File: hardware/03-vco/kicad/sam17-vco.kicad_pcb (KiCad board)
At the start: 2 copper layers, 240 x 172 mm, 140 parts, among them J1 Molex_KK-254_AE-6410-04A_1x04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, J2 IDC-Header_2x06_P2.54mm_Verti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, U1 QFN-32-1EP_4x4mm_P0.4mm_EP2.6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, U10 SOIC-14_3.9x8.7mm_P1.27mm, U11 SOT-89-3, U12 SOT-223-3_TabPin2, U13 VSSOP-8_3x3mm_P0.65mm, U14 SOT-23-5, U2 QFN-32-1EP_4x4mm_P0.4mm_EP2.6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, U3 QFN-32-1EP_4x4mm_P0.4mm_EP2.6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, U4 QFN-32-1EP_4x4mm_P0.4mm_EP2.6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, U5 TSSOP-16_4.4x5mm_P0.65mm, U6 TSSOP-16_4.4x5mm_P0.65mm, U7 TSSOP-16_4.4x5mm_P0.65mm, U8 SOIC-8_3.9x4.9mm_P1.27mm, U9 SOIC-14_3.9x8.7mm_P1.27mm

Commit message: Modulo 3 VCO: cuadro 2x2 y ruteo con Freerouting (Tarea 6, ronda 2)
La causa raiz de la tanda anterior era el desparramo: 4 voces en fila sobre
240x172 mm dejaban el DAC de tono a 85 mm de la voz mas lejana -- 70% por
encima de los 50 mm que modela dac_local_budget.LARGO_LOCAL -- y creaban los
cuellos de ruteo de propina. Aqui las voces van en CUADRO 2x2 con los tres
DAC y la referencia en el hueco central: las cuatro quedan a la misma
distancia, el peor par baja a 41.8 mm (37.7 el de U5, el que manda la
afinacion) y la placa cabe en 114x118 mm, 3.1x menos area. El suelo de
afinacion pasa de 0.635 a 0.5665 cents contra el limite de 0.7.

La fila de abajo va girada 180 grados, y no por simetria: cada lado del QFN
lleva senales fijas, y girando las voces 2 y 4 los cuatro R_MIX y R_PITCH
miran al centro (5 buses ganados) contra VREF_2V5 y PWM_CV que pasan afuera.

El ruteador casero de caminos en L/Z se va entero (~230 lineas) y lo
sustituye Freerouting headless: exportar DSN desde pcbnew, correr el jar,
importar el SES, repetir desde el resultado anterior y quedarse con la mejor
ronda. Tres cosas que costaron encontrarse y quedan documentadas en el
script: -mt 1 es obligatorio (su optimizador multihilo esta roto y admite
estarlo), la 2.2.x/2.3.0 piden Java 25, y el FANOUT viene apagado de fabrica
-- encenderlo, con todo lo demas igual, bajo los tramos sin cerrar de 31 a
11. Como no hay flag de CLI para eso, ajustes_freerouting() parchea las tres
claves que importan del freerouting.json del usuario.

coser_masas() baja cada pad de masa al plano con su propia via DESPUES de
rutear: todo el cobre es SMD en F.Cu y sin via un pad de GNDA mira el
vertido sin tocarlo. Metidas antes del router, esas vias multiplican por
doce el tiempo de cada pasada sin aportar nada al ruteo de senal.

NO CIERRA, y el script sale con error: quedan 18 conexiones de ~500 y el
plano analogico acaba en 30 islas con el 96.5% del cobre en la mayor. Las
dos cosas son el mismo problema y esta acotado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
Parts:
- moved C26 173.4 mm to (64.0, 92.0)
- moved TP2 168.3 mm to (64.0, 96.0)
- moved C25 159.7 mm to (70.0, 92.0)
- moved TP1 152.2 mm to (70.0, 96.0)
- moved H4 137.1 mm to (108.0, 112.0)
- moved J1 136.3 mm to (94.0, 108.0)
- moved C8 132.3 mm to (78.0, 92.0)
- moved C9 127.8 mm to (98.0, 100.0)
- moved U11 127.8 mm to (84.0, 92.0)
- moved H2 126.0 mm to (108.0, 6.00)
- moved C10 125.6 mm to (89.0, 92.0)
- moved U12 123.7 mm to (98.0, 93.0)
- moved TP3 122.8 mm to (78.0, 96.0)
- moved TP4 120.8 mm to (86.0, 100.0)
- moved R_SCALE4 118.1 mm to (83.0, 77.0), turned to 180 degrees
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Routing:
- net GNDA: track 0.00 -> 311.0 mm, vias 0 -> 97
- net PWM_CV: track 0.00 -> 238.1 mm, vias 0 -> 10
- net -12V: track 66.0 -> 302.6 mm, vias 0 -> 10
- net VREF_2V5: track 178.8 -> 395.6 mm, vias 0 -> 12
- net +5V_LOC: track 133.3 -> 338.8 mm, vias 2 -> 16
- net SPI_SCLK: track 0.00 -> 186.6 mm, vias 0 -> 5
- net MIX_SINE: track 52.0 -> 220.6 mm, vias 2 -> 8
- net SPI_CS3: track 0.00 -> 167.8 mm, vias 0 -> 8
- net SQ_3: track 0.00 -> 158.1 mm, vias 0 -> 5
- net VOICE_OUT_1: track 190.1 -> 39.0 mm, vias 2 -> 1
- net CV_PITCH_3: track 6.29 -> 144.4 mm, vias 0 -> 2
- net SPI_MOSI: track 0.00 -> 112.7 mm, vias 0 -> 4
- net SQ_1: track 0.00 -> 111.0 mm, vias 0 -> 3
- net SQ_4: track 0.00 -> 104.9 mm, vias 0 -> 2
- net CV_PITCH_2: track 6.29 -> 86.6 mm, vias 0 -> 4
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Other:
- board size 240 x 172 mm -> 114 x 118 mm

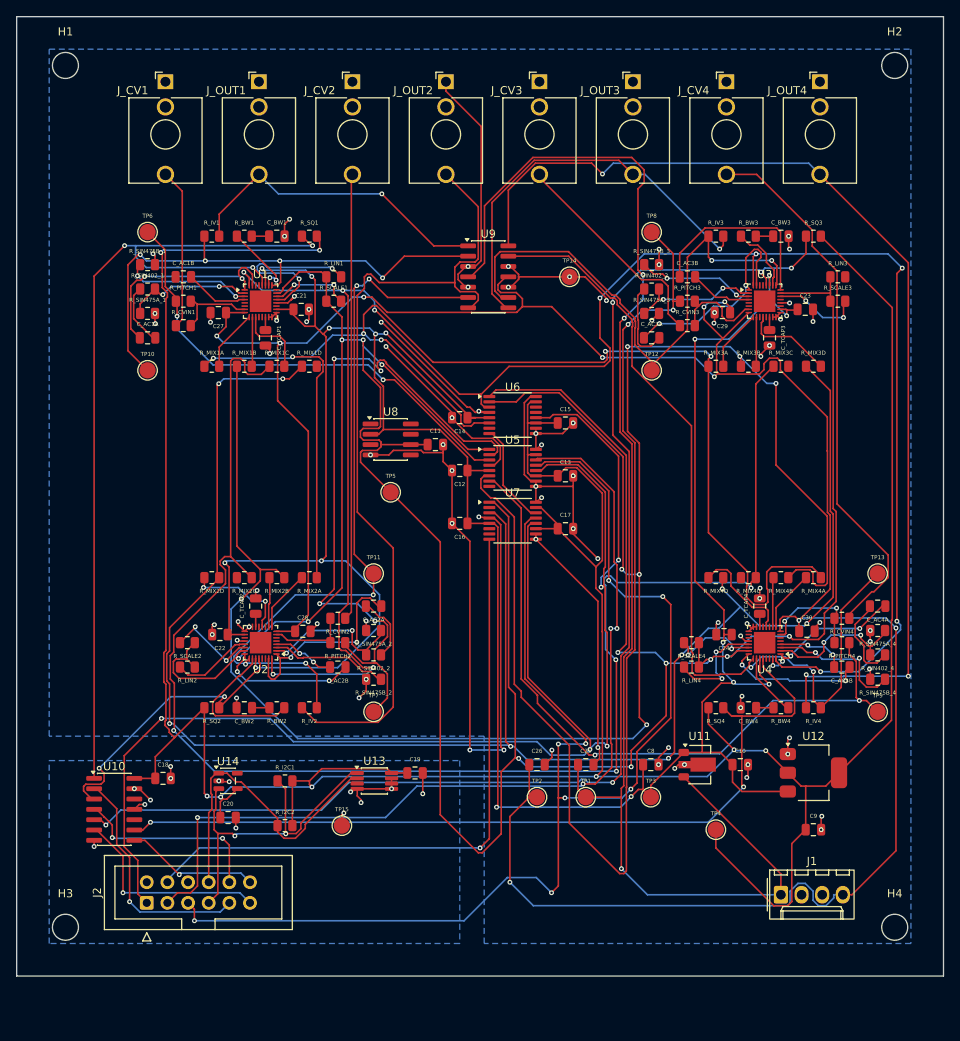
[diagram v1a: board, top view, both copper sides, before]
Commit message: Modulo 3 VCO: la placa pasa a 4 capas (Tarea 6, ronda 3)
Ruling del controlador sobre el BLOCKED de la ronda anterior. La evidencia
de las once configuraciones medidas mostraba que el grafo de esta placa no
es plano y que en 2 capas la unica capa donde cruzar era el propio plano de
masa: cada cruce, una ranura. Ni el spec ni ninguna asercion exigian 2
capas -- era calco de placas mas simples.

El stackup nuevo:

    F.Cu     senal
    In1.Cu   GNDA solida, sin una sola pista
    In2.Cu   GNDD (la esquina de la isla) + potencia
    B.Cu     senal

Y el presupuesto MEJORA con el cambio, no solo el ruteo: dac_local_budget.py
modela el camino DAC->VCO sobre un vertido de 20 mm de ancho, y lo que hay
ahora debajo de ese camino es una capa interna entera y sin cortes. La
asimetria vieja de B.Cu se va con el motivo que la sostenia; la regla nueva
es que In1 no se toca, y se comprueba por partida doble: cero pistas en In1,
y la isla mayor del vertido con mas del 99% del cobre.

Tres cosas que costaron encontrarse y quedan documentadas en el script:

- Un area de reglas de KiCad sobre In1 no vale: se exporta como wire_keepout
  de placa entera y Freerouting se atasca en seco, 200 conexiones sin rutear
  desde la pasada 4 hasta la 139 sin moverse. Lo que si entiende es el
  idioma de Specctra, marcar la capa como (type power); con eso baja de 222
  a 80 en 14 pasadas. Como KiCad no sabe exportar eso, _ajustar_dsn() lo
  parchea en el DSN temporal.
- El router redondea y dejaba pistas a 0.1480 mm apuntando a 0.15: una
  infraccion de DRC por aritmetica. El mismo parche le pide 0.16 mientras el
  DRC sigue exigiendo 0.15.
- El anillo de la voz venia demasiado apretado del apuro de 2 capas y seis
  conexiones locales del QFN no encontraban salida. Con 4 capas hay sitio
  para pagarlo: la celda pasa de 26.4x20.1 a 28.7x22.3 mm.

coser_masas() tenia cuatro bugs, y el ultimo es el que importa: daba por
resuelto un pad que tuviera una via de su red a menos de 1.2 mm. Cercania no
es 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
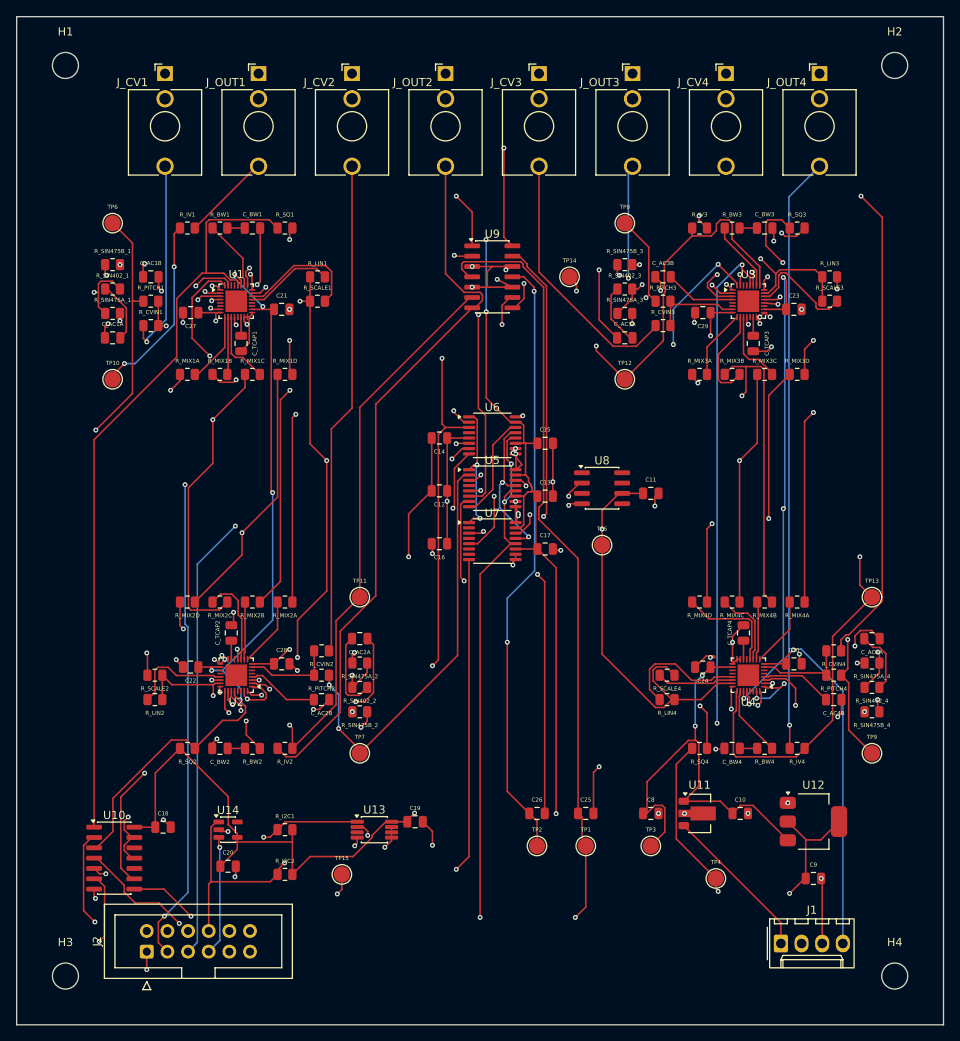
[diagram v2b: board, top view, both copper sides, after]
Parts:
- moved C11 27.2 mm to (78.0, 58.6)
- moved TP5 26.8 mm to (72.0, 65.0)
- moved U8 26.7 mm to (72.0, 58.0)
- moved C10 6.00 mm to (89.0, 98.0)
- moved C18 6.00 mm to (18.0, 99.7)
- moved C19 6.00 mm to (49.0, 99.0)
- moved C20 6.00 mm to (26.0, 104.5)
- moved C25 6.00 mm to (70.0, 98.0)
- moved C26 6.00 mm to (64.0, 98.0)
- moved C8 6.00 mm to (78.0, 98.0)
- moved C9 6.00 mm to (98.0, 106.0)
- moved H3 6.00 mm to (6.00, 118.0)
- moved H4 6.00 mm to (108.0, 118.0)
- moved J1 6.00 mm to (94.0, 114.0)
- moved J2 6.00 mm to (16.0, 115.0)
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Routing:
- net GNDA: track 311.0 -> 154.2 mm, vias 97 -> 71
- net VREF_2V5: track 395.6 -> 257.8 mm, vias 12 -> 9
- net MIX_SAW: track 238.3 -> 136.3 mm, vias 7 -> 4
- net MIX_SINE: track 220.6 -> 131.8 mm, vias 8 -> 4
- net CV_PITCH_3: track 144.4 -> 58.9 mm
- net +3V3_LOC: track 399.3 -> 321.1 mm
- net SPI_SCLK: track 186.6 -> 111.0 mm, vias 5 -> 4
- net SPI_CS3: track 167.8 -> 108.8 mm, vias 8 -> 3
- net MIX_PULSE: track 188.2 -> 135.3 mm, vias 4 -> 3
- net +5V_LOC: track 338.8 -> 293.5 mm, vias 16 -> 15
- net -12V: track 302.6 -> 261.1 mm, vias 10 -> 6
- net PWM_CV: track 238.1 -> 197.0 mm, vias 10 -> 7
- net CV_PITCH_2: track 86.6 -> 51.3 mm, vias 4 -> 2
- net +12V: track 170.6 -> 140.7 mm, vias 3 -> 1
- net CV_PITCH_1: track 58.5 -> 81.0 mm
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- added copper zone on In1.Cu, net GNDA
- added copper zone on In2.Cu, net GNDD
- removed copper zone on B.Cu, net GNDA
- removed copper zone on B.Cu, net GNDD
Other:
- board size 114 x 118 mm -> 114 x 124 mm
- copper layers 2 -> 4

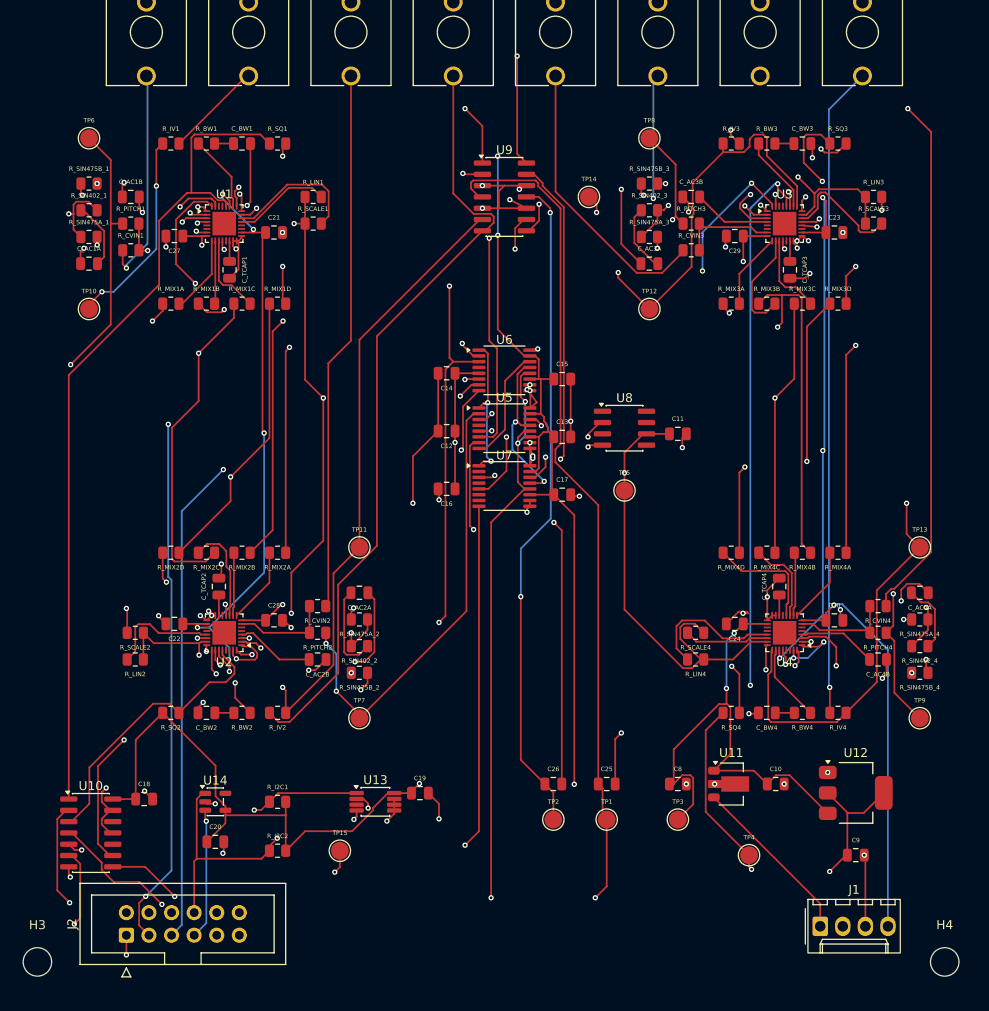
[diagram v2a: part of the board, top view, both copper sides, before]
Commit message: Modulo 3 VCO: costuras de masa reservadas y In2 protegida (Tarea 6, ronda 4)
Las 8 conexiones abiertas de la ronda anterior eran todas pads de masa, y
quedan cerradas por los dos caminos que autorizo el controlador.

COSTURAS_RESERVADAS: siete vias de masa que el script coloca ANTES de
rutear, con el motivo de cada una escrito al lado. Son los pines 20 de los
cuatro QFN (costado derecho, con un vecino de otra red a 0.4 mm por arriba y
otro por abajo, y el desacoplo de +5V cerrando el pasillo) y los pines 4 de
los tres TSSOP (hueco de 1.45 mm contra su propio desacoplo). La clave es el
orden, no la coordenada: puestas antes, el router las ve como obstaculo y da
la vuelta; puestas despues no hay por donde. Y siete vias el modelo del
router apenas las nota -- con las ~95 de toda la placa, cada pasada pasaba
de 15 s a tres minutos. Para que no se las levante, _ajustar_dsn() marca
ahora el cobre de masa como (type protect) en vez del (type route) que
exporta KiCad. coser_masas() pasa de dejar 6 pads sin sitio a dejar cero.

Ademas, el vertido de GNDD aparecia partido en dos: In2 lleva la potencia Y
el retorno digital, y el ruteo de potencia lo cruzaba. Un area de reglas en
In2, solo dentro de la esquina de la isla, lo deja de una pieza; la potencia
vive en el rincon opuesto y no necesita pasar por ahi.

via_costs baja de 30 a 8. El 30 venia de la placa de 2 capas, donde bajar
era caro de verdad; con dos capas de senal y un plano solido en medio,
penalizar el cambio de capa solo consigue que el router se ahogue en el
anillo de un QFN de 0.4 mm en vez de escapar hacia abajo. En la misma placa:
de ~40 conexiones sin cerrar a 24.

Queda anotado un experimento que salio mal y se revierte: mover C_5V del pin
18 (costado derecho) al 27 (arriba) para despejar el abanico de VREF dio
PEOR resultado -- 8 abiertas contra 5. Lo que despeja de un lado lo tapa del
otro. Va documentado en el script para que nadie lo repita a ciegas.

DONDE QUEDA: DRC 0, In1 sin pistas y al 99.97% en una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
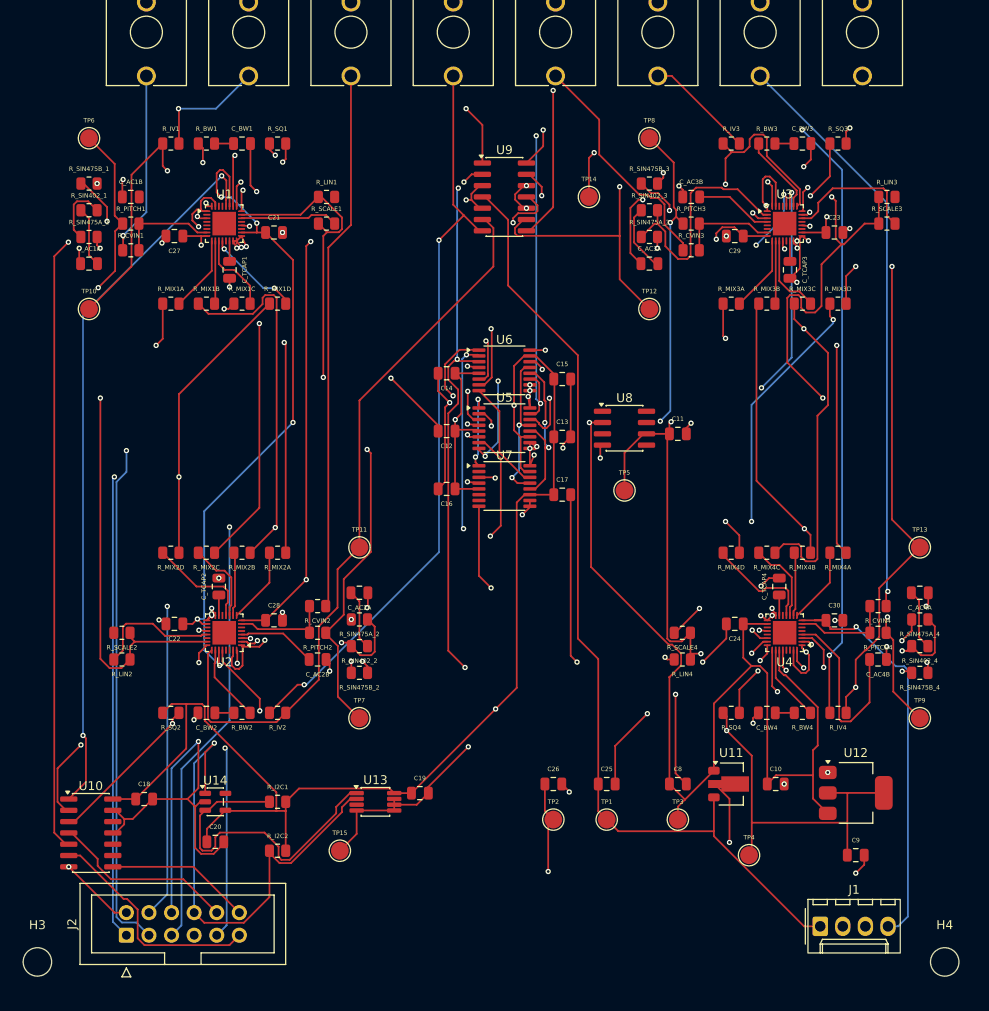
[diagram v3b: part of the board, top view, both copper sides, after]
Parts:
- moved R_LIN1 1.50 mm to (38.5, 32.0)
- moved R_LIN2 1.50 mm to (15.5, 84.0)
- moved R_LIN3 1.50 mm to (101.5, 32.0)
- moved R_LIN4 1.50 mm to (78.5, 84.0)
- moved R_SCALE1 1.50 mm to (38.5, 35.0)
- moved R_SCALE2 1.50 mm to (15.5, 81.0)
- moved R_SCALE3 1.50 mm to (101.5, 35.0)
- moved R_SCALE4 1.50 mm to (78.5, 81.0)
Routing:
- net GNDD: track 22.1 -> 112.6 mm, vias 11 -> 4
- net SQ_4: track 100.3 -> 11.2 mm, vias 3 -> 2
- net MIX_TRI: track 151.5 -> 116.0 mm
- net VREF_2V5: track 257.8 -> 292.8 mm, vias 9 -> 11
- net +12V: track 140.7 -> 109.1 mm, vias 1 -> 0
- net -12V: track 261.1 -> 286.0 mm, vias 6 -> 7
- net I2C_SCL: track 38.1 -> 55.3 mm, vias 2 -> 1
- net TUNE_OUT_1: track 30.1 -> 47.1 mm, vias 1 -> 2
- net N2_1: track 23.7 -> 7.17 mm, vias 2 -> 0
- net GNDA: track 154.2 -> 170.1 mm, vias 71 -> 82
- net MIX_SAW: track 136.3 -> 152.0 mm
- net +5V_LOC: track 293.5 -> 308.7 mm, vias 15 -> 10
- net N21_4: track 15.7 -> 1.14 mm, vias 0 -> 1
- net VOICE_OUT_4: track 125.4 -> 110.9 mm, vias 2 -> 3
- net N22_2: track 13.2 -> 0.00 mm, vias 2 -> 0
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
